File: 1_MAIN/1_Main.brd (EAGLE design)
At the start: 67.4 x 54.8 mm, 40 parts, among them IC1 NCP1117-33ST, IC10 FT232RL, IC7 MAX14932, IC8 MAX14932, IC9 MAX14932, Q1 IRF7416, X14 ALLSERIALMM, X2 MINI-USB-32005-201, X3 AKL18X-04W

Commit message: updated readme & mainboard
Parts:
- moved C2 6.35 mm to (26.7, 12.7)
- moved R4 1.72 mm to (20.3, 11.4)
- moved LED3 1.27 mm to (10.2, 7.62)
- moved U$3 1.27 mm to (10.2, 8.89)
- moved LED2 1.27 mm to (10.2, 5.08)
- moved LED1 1.27 mm to (10.2, 12.7)
- moved LED4 1.27 mm to (10.2, 10.2)
- moved R3 0.55 mm to (16.5, 3.81)
- moved R9 0.43 mm to (16.5, 8.89)
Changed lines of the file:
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@@
 <elements>
 <element name="L10" library="EagleLibrary_Wuerth_Elektronik_eiSos_Version_6-12" package="0805" value="WE-CBF_0805" x="-23.38" y="12.74" rot="R90"/>
-<element name="R3" library="rcl" package="R0805" value="270" x="17.06" y="3.88" rot="R90"/>
-<element name="R4" library="rcl" package="R0805" value="270" x="18.68" y="11.96" rot="R90"/>
-<element name="LED2" library="led" package="CHIPLED_0603" value="RX" x="10.16" y="3.81" rot="R270">
-<attribute name="COLOR" value="GN" x="10.16" y="3.81" size="1.778" layer="27" rot="R270" display="off"/>
-</element>
-<element name="LED3" library="led" package="CHIPLED_0603" value="TX" x="10.16" y="6.35" rot="R270">
-<attribute name="COLOR" value="RD" x="10.16" y="6.35" size="1.778" layer="27" rot="R270" display="off"/>
+<element name="R3" library="rcl" package="R0805" value="270" x="16.51" y="3.81" rot="R90"/>
+<element name="R4" library="rcl" package="R0805" value="270" x="20.32" y="11.43" rot="R90"/>
+<element name="LED2" library="led" package="CHIPLED_0603" value="RX" x="10.16" y="5.08" rot="R270">
+<attribute name="COLOR" value="GN" x="10.16" y="5.08" size="1.778" layer="27" rot="R270" display="off"/>
+</element>
+<element name="LED3" library="led" package="CHIPLED_0603" value="TX" x="10.16" y="7.62" rot="R270">
+<attribute name="COLOR" value="RD" x="10.16" y="7.62" size="1.778" layer="27" rot="R270" display="off"/>
 </element>
 <element name="C1" library="rcl" package="C0805" value="10n" x="-26.67" y="11.43" rot="R180"/>
-<element name="C2" library="rcl" package="C0805" value="100n" x="30.48" y="7.62" rot="R90"/>
+<element name="C2" library="rcl" package="C0805" value="100n" x="26.67" y="12.7" rot="R90"/>
 <element name="C3" library="rcl" package="C0805" value="10µ" x="30.48" y="40.64" rot="R90"/>
 <element name="R8" library="rcl" package="R0805" value="180" x="30.48" y="25.4"/>
-<element name="LED1" library="led" package="CHIPLED_0603" value="PWR" x="10.16" y="11.43" rot="R90">
-<attribute name="COLOR" value="GN" x="10.16" y="11.43" size="1.778" layer="27" rot="R90" display="off"/>
+<element name="LED1" library="led" package="CHIPLED_0603" value="PWR" x="10.16" y="12.7" rot="R90">
+<attribute name="COLOR" value="GN" x="10.16" y="12.7" size="1.778" layer="27" rot="R90" display="off"/>
 </element>
 <element name="C13" library="rcl" package="C0805" value="10µ" x="30.85" y="35.56" rot="R90"/>
@@
 </element>
 <element name="C18" library="rcl" package="C0805" value="100n" x="31.75" y="30.48" rot="R270"/>
-<element name="R9" library="rcl" package="R0805" value="180" x="16.35" y="8.49" rot="R90"/>
-<element name="LED4" library="led" package="CHIPLED_0603" value="TXEN" x="10.16" y="8.89" rot="R90">
-<attribute name="COLOR" value="YE" x="10.16" y="8.89" size="1.778" layer="27" rot="R90" display="off"/>
+<element name="R9" library="rcl" package="R0805" value="180" x="16.51" y="8.89" rot="R90"/>
+<element name="LED4" library="led" package="CHIPLED_0603" value="TXEN" x="10.16" y="10.16" rot="R90">
+<attribute name="COLOR" value="YE" x="10.16" y="10.16" size="1.778" layer="27" rot="R90" display="off"/>
 </element>
 <element name="X2" library="con-cypressindustries" package="32005-201" value="MINI-USB-32005-201" x="-21.59" y="5.08" rot="R90">
@@
 <attribute name="OC_FARNELL" value="unknown" x="3.81" y="26.67" size="1.778" layer="27" display="off"/>
 </element>
-<element name="U$3" library="Mentor" package="1296.1004" value="" x="10.16" y="7.62" rot="R180"/>
+<element name="U$3" library="Mentor" package="1296.1004" value="" x="10.16" y="8.89" rot="R180"/>
 <element name="IC7" library="max14932" package="SO16" value="MAX14932" x="-8.89" y="35.56"/>
 <element name="IC8" library="max14932" package="SO16" value="MAX14932" x="7.62" y="35.56"/>
@@
 <wire x1="22.595" y1="16.695" x2="19.995" y2="16.695" width="0" layer="19" extent="1-1"/>
 <wire x1="20.645" y1="23.945" x2="13.97" y2="21.27" width="0" layer="19" extent="1-1"/>
-<wire x1="9.41" y1="11.43" x2="11.43" y2="21.27" width="0" layer="19" extent="1-1"/>
-<wire x1="9.41" y1="8.89" x2="9.41" y2="11.43" width="0" layer="19" extent="1-1"/>
-<wire x1="20.5994" y1="3.8354" x2="9.41" y2="8.89" width="0" layer="19" extent="1-1"/>
+<wire x1="9.41" y1="12.7" x2="11.43" y2="21.27" width="0" layer="19" extent="1-1"/>
+<wire x1="9.41" y1="10.16" x2="9.41" y2="12.7" width="0" layer="19" extent="1-1"/>
 <wire x1="31.75" y1="29.53" x2="20.645" y2="23.945" width="0" layer="19" extent="1-1"/>
+<wire x1="20.5994" y1="3.8354" x2="19.995" y2="16.695" width="0" layer="19" extent="1-1"/>
 <wire x1="-19.99" y1="8.08" x2="-12.065" y2="32.96" width="0" layer="19" extent="1-1"/>
 <wire x1="-27.62" y1="11.43" x2="-19.99" y2="8.08" width="0" layer="19" extent="1-1"/>
@@
 <contactref element="IC10" pad="23"/>
 <contactref element="R4" pad="2"/>
-<wire x1="18.68" y1="12.91" x2="21.295" y2="16.695" width="0" layer="19" extent="1-1"/>
+<wire x1="20.32" y1="12.38" x2="21.295" y2="16.695" width="0" layer="19" extent="1-1"/>
 </signal>
 <signal name="RXLED">
 <contactref element="IC10" pad="22"/>
 <contactref element="R3" pad="2"/>
-<wire x1="17.06" y1="4.83" x2="20.645" y2="16.695" width="0" layer="19" extent="1-1"/>
+<wire x1="16.51" y1="4.76" x2="20.645" y2="16.695" width="0" layer="19" extent="1-1"/>
 </signal>
 <signal name="N$38">
@@
 <wire x1="-22.86" y1="20" x2="-24.765" y2="21.65" width="0" layer="19" extent="1-1"/>
 <wire x1="31.43" y1="25.4" x2="22.54" y2="39.37" width="0" layer="19" extent="1-1"/>
-<wire x1="9.41" y1="6.35" x2="10.795" y2="32.96" width="0" layer="19" extent="1-1"/>
-<wire x1="9.41" y1="3.81" x2="9.41" y2="6.35" width="0" layer="19" extent="1-1"/>
+<wire x1="9.41" y1="7.62" x2="10.795" y2="32.96" width="0" layer="19" extent="1-1"/>
+<wire x1="9.41" y1="5.08" x2="9.41" y2="7.62" width="0" layer="19" extent="1-1"/>
 </signal>
 <signal name="N$5">
@@
 <contactref element="R4" pad="1"/>
 <contactref element="LED3" pad="C"/>
-<wire x1="10.91" y1="6.35" x2="18.68" y2="11.01" width="0" layer="19" extent="1-1"/>
+<wire x1="10.91" y1="7.62" x2="20.32" y2="10.48" width="0" layer="19" extent="1-1"/>
 </signal>
 <signal name="N$6">
 <contactref element="R3" pad="1"/>
 <contactref element="LED2" pad="C"/>
-<wire x1="10.91" y1="3.81" x2="17.06" y2="2.93" width="0" layer="19" extent="1-1"/>
+<wire x1="10.91" y1="5.08" x2="16.51" y2="2.86" width="0" layer="19" extent="1-1"/>
 </signal>
 <signal name="N$7">
 <contactref element="R9" pad="1"/>
 <contactref element="LED4" pad="A"/>
-<wire x1="10.91" y1="8.89" x2="16.35" y2="7.54" width="0" layer="19" extent="1-1"/>
+<wire x1="10.91" y1="10.16" x2="16.51" y2="7.94" width="0" layer="19" extent="1-1"/>
 </signal>
 <signal name="N$8">
 <contactref element="R8" pad="1"/>
 <contactref element="LED1" pad="A"/>
-<wire x1="10.91" y1="11.43" x2="29.53" y2="25.4" width="0" layer="19" extent="1-1"/>
+<wire x1="10.91" y1="12.7" x2="29.53" y2="25.4" width="0" layer="19" extent="1-1"/>
 </signal>
 <signal name="GND1">
@@
 <wire x1="-11.43" y1="42.545" x2="-12.065" y2="38.16" width="0" layer="19" extent="1-1"/>
 <wire x1="-27.7114" y1="29.9212" x2="-19.05" y2="40.64" width="0" layer="19" extent="1-1"/>
-<wire x1="30.48" y1="8.57" x2="30.85" y2="36.51" width="0" layer="19" extent="1-1"/>
+<wire x1="26.67" y1="13.65" x2="30.85" y2="36.51" width="0" layer="19" extent="1-1"/>
 <wire x1="-9.06" y1="7.62" x2="-2.54" y2="35.88" width="0" layer="19" extent="1-1"/>
 </signal>
@@
 <wire x1="-8.89" y1="46.99" x2="-8.89" y2="45.085" width="0.4064" layer="1"/>
 <contactref element="IC1" pad="3"/>
-<wire x1="30.48" y1="6.67" x2="30.48" y2="39.69" width="0" layer="19" extent="1-1"/>
-<wire x1="-2.06" y1="7.62" x2="30.48" y2="6.67" width="0" layer="19" extent="1-1"/>
+<wire x1="26.67" y1="11.75" x2="30.48" y2="39.69" width="0" layer="19" extent="1-1"/>
+<wire x1="-2.06" y1="7.62" x2="26.67" y2="11.75" width="0" layer="19" extent="1-1"/>
 <wire x1="-23.0886" y1="29.9212" x2="-2.06" y2="7.62" width="0" layer="19" extent="1-1"/>
 <wire x1="-16.51" y1="48.26" x2="-23.0886" y2="29.9212" width="0" layer="19" extent="1-1"/>
@@
 <contactref element="IC9" pad="3"/>
 <wire x1="16.745" y1="23.945" x2="22.92" y2="43.815" width="0" layer="19" extent="1-1"/>
-<wire x1="16.35" y1="9.44" x2="16.745" y2="23.945" width="0" layer="19" extent="1-1"/>
+<wire x1="16.51" y1="9.84" x2="16.745" y2="23.945" width="0" layer="19" extent="1-1"/>
 </signal>
 <signal name="N$13">

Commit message: finish FTDI PCB
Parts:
- removed SV4, SV6: (no value), con-lstb:MA04-2
- added C10, C9: 1µ, rcl:C0805
- added IC2: MCP1700T-1802E, SeeSys:SOT23
- added SV1: (no value), con-harting-ml:ML10
- moved C2 54.0 mm to (-20.3, 39.4), turned to 180 degrees
- moved C3 50.9 mm to (-20.3, 36.8), turned to 180 degrees
- moved C13 46.4 mm to (-15.2, 30.5), turned to 270 degrees
- moved R8 22.7 mm to (10.2, 15.2)
- moved C18 22.0 mm to (17.1, 14.0)
- moved C5 16.1 mm to (27.3, 17.8), turned to 270 degrees
- moved C6 13.5 mm to (27.3, 22.2)
- moved C16 11.7 mm to (26.0, 50.2), turned to 90 degrees
- moved R9 10.2 mm to (6.35, 7.62)
- moved DC1 9.25 mm to (-22.9, 49.5)
- moved C8 6.48 mm to (3.81, 38.1), turned to 180 degrees
- moved R3 6.38 mm to (15.9, 10.2), turned to 0 degrees
- moved DC2 6.25 mm to (-22.9, 42.5)
- moved R4 5.85 mm to (15.9, 7.62), turned to 0 degrees
- moved LED4 5.71 mm to (10.2, 4.45), turned to 270 degrees
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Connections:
- new net +1V8/1: C10.1, IC2.2, X14.14
- net +3V3/1: now also C9.1, IC2.3
- net GND: now also IC7.4, SV1.10; no longer IC9.4
- net GND1: now also C10.2, C9.2, IC2.1, IC8.11; no longer IC9.11
- net N$14: now also SV1.8
- net N$29: now also SV1.5
- net N$3: now also SV1.9
- net N$32: now also SV1.7
- net N$33: now also IC9.4, SV1.2; no longer IC7.4
- net N$34: now also IC9.6; no longer IC8.5
- net N$35: now also SV1.6
- net N$36: now also IC8.5, SV1.4; no longer IC8.6
- net N$84: now also IC9.13; no longer IC7.13
- net N$85: now also IC9.11; no longer IC8.12
- net N$87: now also IC8.12; no longer IC8.11
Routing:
- net +5V: track 7.62 -> 162.4 mm, vias 0 -> 9
- net +3V3/1: track 0.00 -> 74.3 mm, vias 0 -> 1
- net N$38: track 0.00 -> 68.6 mm
- net N$3: track 0.00 -> 66.7 mm, vias 0 -> 2
- net VIN1: track 0.00 -> 59.9 mm, vias 0 -> 6
- net GND1: track 0.00 -> 59.1 mm, vias 0 -> 10
- net +5V/1: track 10.1 -> 59.4 mm, vias 0 -> 1
- net N$19: track 0.00 -> 46.9 mm
- net +12V/1: track 8.75 -> 53.4 mm
- net N$21: track 0.00 -> 43.4 mm
- net N$33: track 0.00 -> 42.3 mm, vias 0 -> 2
- net N$14: track 0.00 -> 42.0 mm, vias 0 -> 2
- net !PWEN: track 0.00 -> 38.0 mm, vias 0 -> 2
- net N$29: track 0.00 -> 37.5 mm, vias 0 -> 2
- net GND: track 0.00 -> 37.0 mm, vias 0 -> 19
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
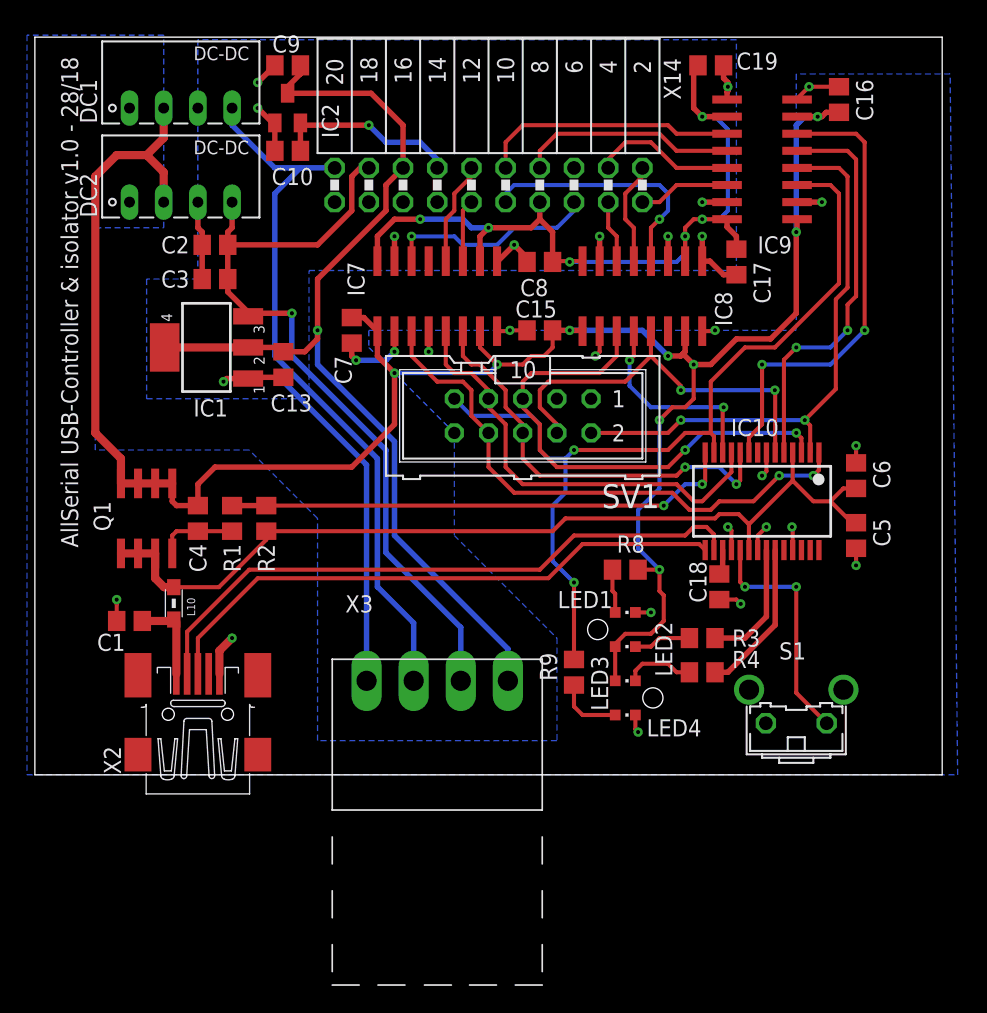
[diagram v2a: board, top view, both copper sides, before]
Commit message: fix connector for LA
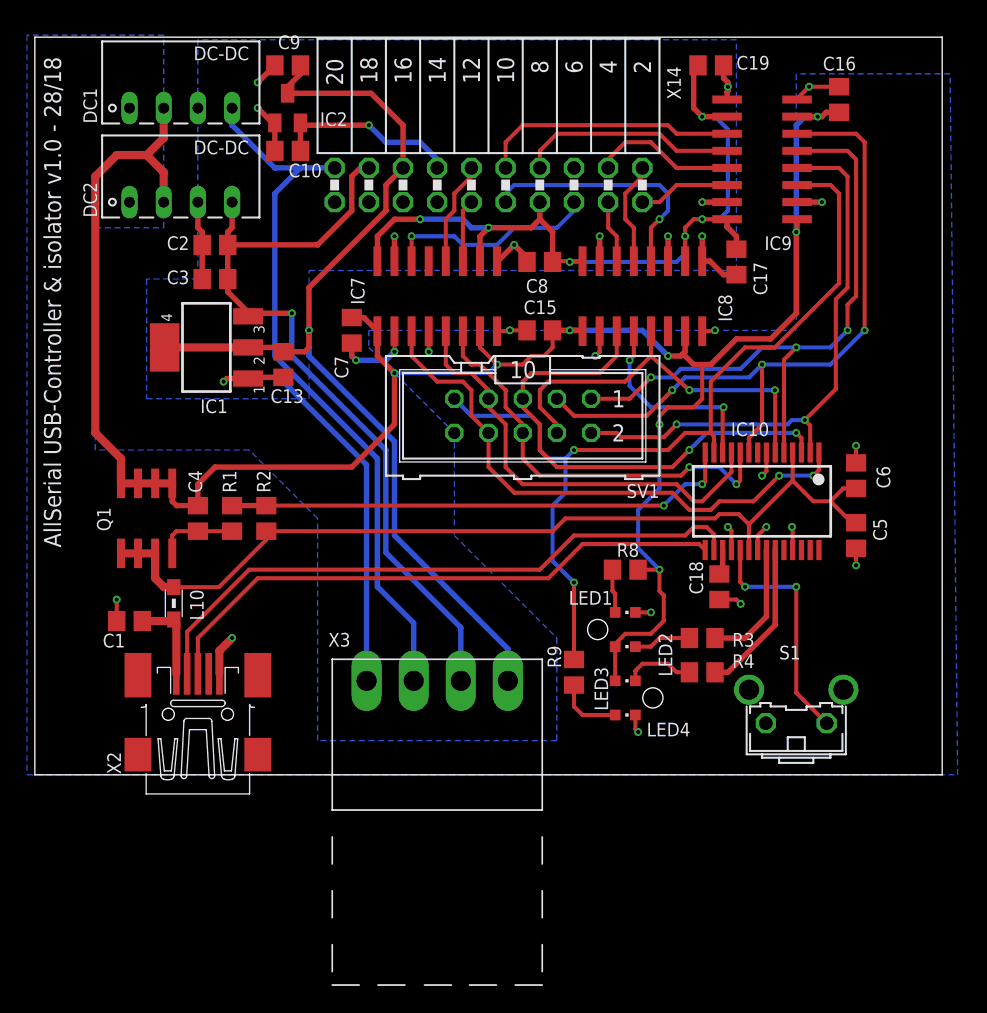
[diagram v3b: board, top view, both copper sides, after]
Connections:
- removed net N$20: IC10.5, IC9.5
- removed net N$34: IC10.9, IC9.6
- new net N$1: IC10.5, IC9.5, SV1.1
- new net N$2: IC10.9, IC9.6, SV1.3
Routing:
- net N$2: track 0.00 -> 52.2 mm, vias 0 -> 3
- net N$1: track 0.00 -> 46.9 mm, vias 0 -> 3
- net N$34: track 34.9 -> 0.00 mm, vias 2 -> 0
- net N$20: track 30.1 -> 0.00 mm, vias 2 -> 0
- net +5V: track 162.4 -> 163.2 mm, vias 9 -> 8

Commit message: Add ESD protection
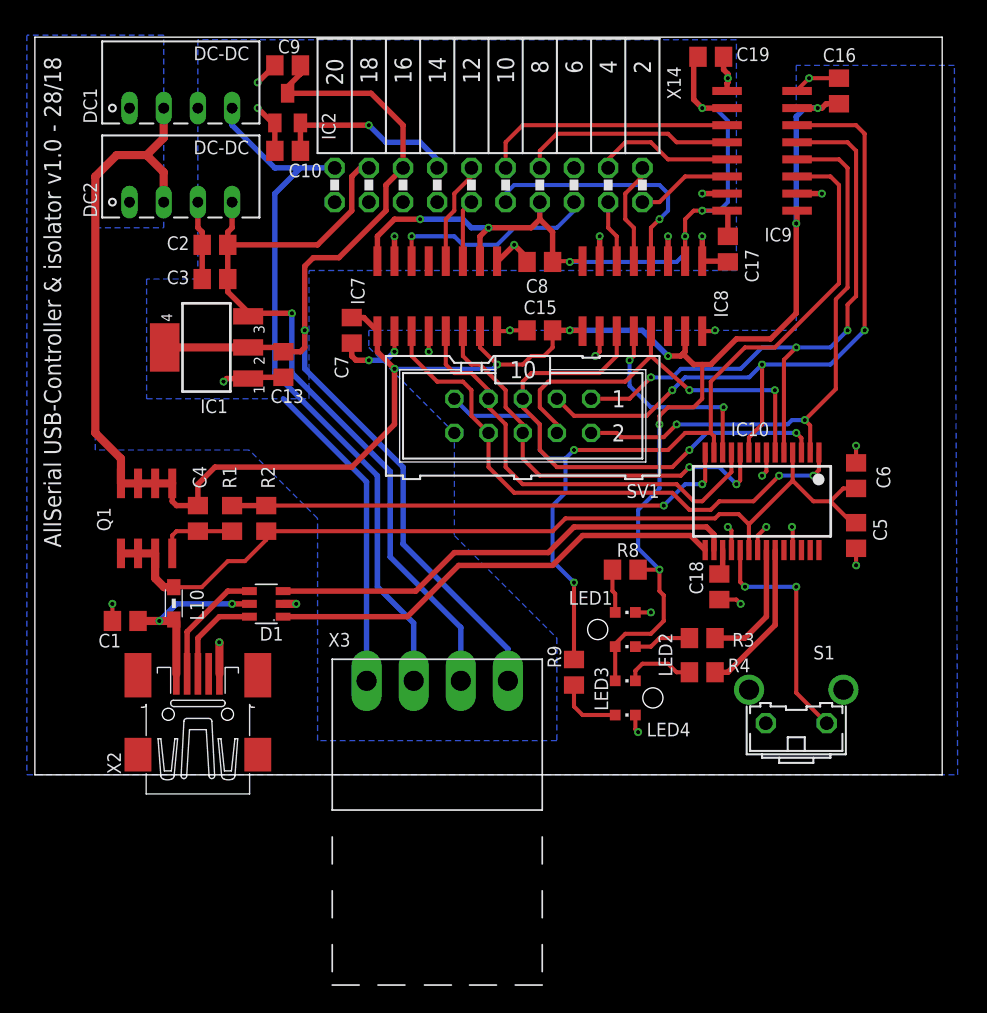
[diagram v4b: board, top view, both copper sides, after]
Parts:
- added D1: USBLC6-2, EagleLibrary_Wuerth_Elektronik_eiSos_Version_6-9:WE-TVS_SOT23-6L
- moved C17 1.14 mm to (17.8, 39.1)
- moved C19 0.64 mm to (16.5, 53.3)
- moved C16 0.63 mm to (26.0, 50.8)
- moved IC9 0.63 mm to (20.3, 46.4)
- moved C1 0.32 mm to (-27.0, 11.4)
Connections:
- removed net N$19: IC10.16, X2.2
- removed net N$21: IC10.15, X2.3
- new net N$10: D1.1, IC10.15
- new net N$12: D1.4, X2.2
- new net N$15: D1.6, X2.3
- new net N$9: D1.3, IC10.16
- net GND: now also D1.2
- net N$11: now also D1.5
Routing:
- net N$19: track 46.9 -> 0.00 mm
- net N$21: track 43.4 -> 0.00 mm
- net N$9: track 0.00 -> 35.4 mm
- net N$10: track 0.00 -> 34.3 mm
- net N$12: track 0.00 -> 9.01 mm
- net N$11: track 6.50 -> 14.0 mm, vias 0 -> 2
- net N$15: track 0.00 -> 7.15 mm
- net GND1: track 59.1 -> 56.9 mm
- net +3V3/1: track 74.6 -> 75.6 mm
- net N$3: track 66.7 -> 67.4 mm
- net N$1: track 46.9 -> 47.6 mm
- net N$33: track 42.5 -> 43.2 mm
- net N$2: track 52.2 -> 52.8 mm
- net +5V: track 163.2 -> 163.7 mm
- net GND: vias 19 -> 20
